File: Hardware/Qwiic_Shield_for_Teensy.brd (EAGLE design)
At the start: 17.8 x 61 mm, 42 parts, among them J1 QWIIC_RA, J2 QWIIC_RA, J3 QWIIC_Vertical, J4 QWIIC_Vertical, J5 ALT PWR

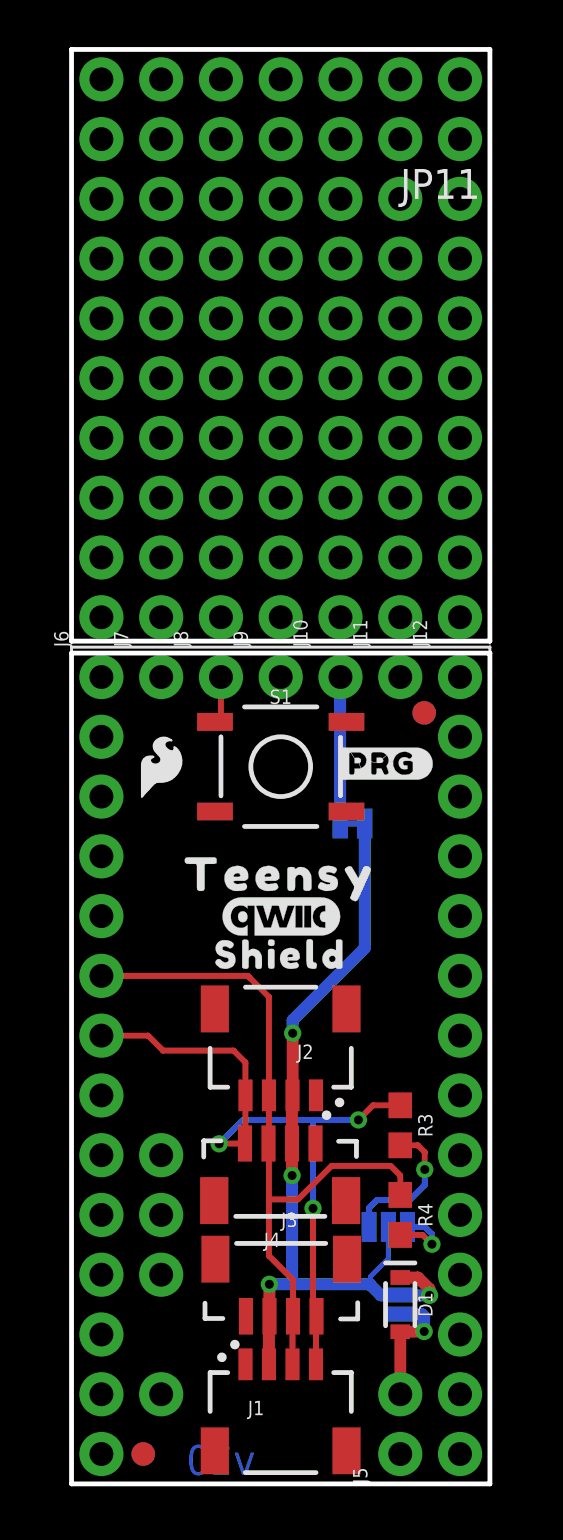
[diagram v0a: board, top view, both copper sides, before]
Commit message: Post group review changes - short version
-"slave" terminology needs to be updated to "I2C peripheral"
-Moving to two separate products. One short and one long. Resolves the prog button access pin difference. no vscores.
-Switch up qwiic connector positions so that the north RA connector doesn't conflict with the prog button.
-3.3V power should come from the PTH header pin on the side (not the middle row).
-Added teensy qwiic shield product name to bottom silk
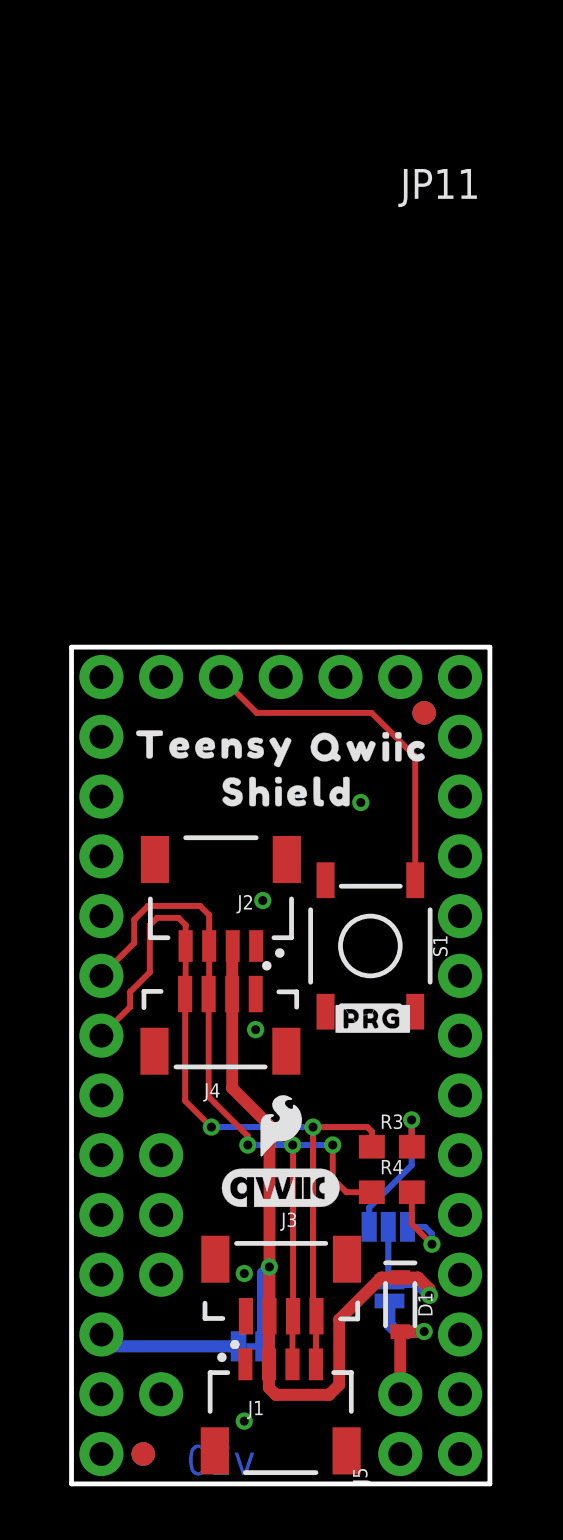
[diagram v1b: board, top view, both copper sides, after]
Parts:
- removed J10, J11, J12, J6, J7, J8, J9: (no value), SparkFun-Connectors:1X10_NO_SILK
- removed U$14: (no value), output:SHIELD0
- removed U$17: (no value), output:#GND#0
- added U$10: (no value), output:#ISO#0
- added U$11, U$9: (no value), output:QWIIC0
- added U$12, U$8: (no value), output:SHIELD0
- U$2: device output:#3V3_ISO#0 -> output:TEENSY0
- moved U$15 28.0 mm to (5.92, 6.38), turned to 0 degrees
- moved 3V3_ISO 22.6 mm to (7.62, 5.84)
- moved LOGO2 16.1 mm to (8.89, 15.2)
- moved LOGO4 11.5 mm to (8.86, 12.6)
- moved U$6 10.9 mm to (12.8, 19.8)
- moved LOGO1 9.26 mm to (8.94, 28.8), turned to 0 degrees
- moved S1 8.52 mm to (12.7, 22.9), turned to 270 degrees
- moved J4 6.84 mm to (6.35, 21.6)
- moved J2 6.84 mm to (6.35, 22.9)
- moved U$13 6.16 mm to (6.15, 31.4)
- moved LOGO3 5.11 mm to (8.89, 17.8), turned to 0 degrees
- moved U$2 1.52 mm to (11.7, 26.7)
- moved R4 1.03 mm to (13.6, 12.4), turned to 0 degrees
- moved R3 0.98 mm to (13.6, 14.3), turned to 0 degrees
- moved D1_BP 0.72 mm to (13.5, 8.18)
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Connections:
- removed net 3V: JP11.3V
- new net NC: JP11.3.3V
- net N$3: now also JP11.3V; no longer JP11.3.3V
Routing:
- net N$5: track 2.01 -> 14.9 mm
- net SCL: track 30.0 -> 34.1 mm, vias 3 -> 2
- net 3.3V: track 35.8 -> 38.4 mm, vias 4 -> 2
- net SDA: track 30.7 -> 33.3 mm, vias 0 -> 3
- net N$1: track 3.11 -> 4.16 mm
- net N$4: track 5.37 -> 6.28 mm
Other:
- board size 17.8 x 61 mm -> 17.8 x 35.6 mm

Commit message: Library updates, name prefix fix, measures update
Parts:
- removed JP11: TEENSY, SparkFun-Boards:TEENSY-3.1_NOSILK
- added J6: ALT PWR, SparkFun-Connectors:1X02_NO_SILK
- J1: value QWIIC_RA -> TEENSY; device SparkFun-Connectors:JST04_1MM_RA -> teensy_boards:TEENSY_NOSILK
- J3: value QWIIC_Vertical -> QWIIC_RA; device SparkFun-Connectors:JST04_1MM_VERT -> SparkFun-Connectors:JST04_1MM_RA
- J5: value ALT PWR -> QWIIC_Vertical; device SparkFun-Connectors:1X02_NO_SILK -> SparkFun-Connectors:JST04_1MM_VERT
- moved J5 21.7 mm to (6.35, 21.6), turned to 180 degrees
- moved J2 18.0 mm to (8.89, 5.08), turned to 0 degrees
- moved J3 16.7 mm to (6.35, 22.9), turned to 180 degrees
- moved J4 15.5 mm to (8.89, 6.35), turned to 0 degrees
- moved J1 12.7 mm to (8.89, 17.8)
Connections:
- net 3.3V: now also J5.2; no longer J1.2
- net GND: now also J1.AGND, J1.GND, J1.GND1, J6.1; no longer J1.1, JP11.AGND, JP11.GND, JP11.GND1
- net N$3: now also J1.3V; no longer JP11.3V
- net N$4: now also J6.2; no longer J5.2
- net N$5: now also J1.PROG; no longer JP11.PROG
- net NC: now also J1.3.3V; no longer JP11.3.3V
- net SCL: now also J1.19, J5.4; no longer J1.4, JP11.19
- net SDA: now also J1.18, J5.3; no longer J1.3, JP11.18
- net VBAT: now also J1.VBAT; no longer JP11.VBAT
- net VIN: now also J1.VIN; no longer JP11.VIN
- net VUSB: now also J1.VUSB; no longer JP11.VUSB
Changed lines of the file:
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@@
 <drawing>
 <settings>
-<setting alwaysvectorfont="yes"/>
+<setting alwaysvectorfont="no"/>
 <setting verticaltext="up"/>
 </settings>
@@
 <layer number="45" name="Holes" color="7" fill="1" visible="yes" active="yes"/>
 <layer number="46" name="Milling" color="3" fill="1" visible="no" active="yes"/>
-<layer number="47" name="Measures" color="7" fill="1" visible="no" active="yes"/>
+<layer number="47" name="Measures" color="7" fill="1" visible="yes" active="yes"/>
 <layer number="48" name="Document" color="7" fill="1" visible="no" active="yes"/>
 <layer number="49" name="Reference" color="7" fill="1" visible="yes" active="yes"/>
@@
 <wire x1="0" y1="35.56" x2="0" y2="0" width="0.2032" layer="20"/>
 <wire x1="0" y1="35.56" x2="17.78" y2="35.56" width="0.2032" layer="20"/>
-<dimension x1="0" y1="0" x2="0" y2="60.96" x3="-22.86" y3="30.48" textsize="1.778" layer="47" unit="inch" visible="yes"/>
-<dimension x1="0" y1="0" x2="0" y2="35.56" x3="-17.78" y3="17.78" textsize="1.778" layer="47" unit="inch" visible="yes"/>
-<dimension x1="0" y1="60.96" x2="17.78" y2="60.96" x3="8.89" y3="68.58" textsize="1.778" layer="47" unit="inch" visible="yes"/>
-<dimension x1="8.89" y1="30.48" x2="8.89" y2="0" x3="-12.7" y3="15.24" textsize="1.778" layer="47" unit="inch" visible="yes"/>
+<dimension x1="0" y1="0" x2="0" y2="35.56" x3="-22.86" y3="17.78" textsize="1.778" layer="47" unit="inch" visible="yes"/>
+<dimension x1="0" y1="35.56" x2="17.78" y2="35.56" x3="8.89" y3="49.53" textsize="1.778" layer="47" unit="inch" visible="yes"/>
 <dimension x1="9.271" y1="8.9408" x2="9.271" y2="0" x3="-2.54" y3="4.4704" textsize="1.27" layer="47" unit="inch" visible="yes"/>
-<dimension x1="9.271" y1="13.1064" x2="9.271" y2="0" x3="-7.747" y3="6.5532" textsize="1.27" layer="47" unit="inch" visible="yes"/>
 <rectangle x1="13.208" y1="0.5842" x2="15.9512" y2="1.9558" layer="22"/>
+<dimension x1="12.7" y1="22.86" x2="17.78" y2="0" x3="39.37" y3="11.43" textsize="1.778" layer="47" dtype="vertical" unit="inch" visible="yes"/>
+<dimension x1="12.7" y1="22.86" x2="0" y2="38.1" x3="6.35" y3="45.72" textsize="1.778" layer="47" dtype="horizontal" unit="inch" visible="yes"/>
+<dimension x1="6.35" y1="22.86" x2="0" y2="41.91" x3="3.175" y3="38.1" textsize="1.778" layer="47" dtype="horizontal" unit="inch" visible="yes"/>
+<dimension x1="6.5278" y1="25.3746" x2="-12.7" y2="0" x3="-11.43" y3="12.6873" textsize="1.778" layer="47" dtype="vertical" unit="inch" visible="yes"/>
+<dimension x1="6.3754" y1="19.0246" x2="-6.35" y2="0" x3="-16.51" y3="9.5123" textsize="1.778" layer="47" dtype="vertical" unit="inch" visible="yes"/>
 </plain>
 <attributes>
@@
 <attribute name="REV" value="" x="-12.7" y="-12.7" size="1.778" layer="27" display="off"/>
 </element>
-<element name="J1" library="SparkFun-Connectors" package="JST04_1MM_RA" value="QWIIC_RA" x="8.89" y="5.08" smashed="yes">
+<element name="J2" library="SparkFun-Connectors" package="JST04_1MM_RA" value="QWIIC_RA" x="8.89" y="5.08" smashed="yes">
 <attribute name="NAME" x="7.493" y="2.921" size="0.6096" layer="25" font="vector" ratio="20"/>
 <attribute name="PROD_ID" value="CONN-13694" x="8.89" y="5.08" size="1.778" layer="27" display="off"/>
 <attribute name="VALUE" x="7.239" y="1.778" size="0.6096" layer="27" font="vector" ratio="20"/>
 </element>
-<element name="J2" library="SparkFun-Connectors" package="JST04_1MM_RA" value="QWIIC_RA" x="6.35" y="22.86" smashed="yes" rot="R180">
+<element name="J3" library="SparkFun-Connectors" package="JST04_1MM_RA" value="QWIIC_RA" x="6.35" y="22.86" smashed="yes" rot="R180">
 <attribute name="NAME" x="7.747" y="25.019" size="0.6096" layer="25" font="vector" ratio="20" rot="R180"/>
 <attribute name="PROD_ID" value="CONN-13694" x="6.35" y="22.86" size="1.778" layer="27" rot="R180" display="off"/>
 <attribute name="VALUE" x="8.001" y="26.162" size="0.6096" layer="27" font="vector" ratio="20" rot="R180"/>
 </element>
-<element name="J4" library="SparkFun-Connectors" package="JST04_1MM_VERT" value="QWIIC_Vertical" x="6.35" y="21.59" smashed="yes" rot="R180">
+<element name="J5" library="SparkFun-Connectors" package="JST04_1MM_VERT" value="QWIIC_Vertical" x="6.35" y="21.59" smashed="yes" rot="R180">
 <attribute name="NAME" x="6.334" y="17.02366875" size="0.6096" layer="25" rot="R180"/>
 <attribute name="PROD_ID" value="CONN-14483" x="6.35" y="21.59" size="1.778" layer="27" rot="R180" display="off"/>
@@
 <element name="FD4" library="SparkFun-Aesthetics" package="FIDUCIAL-1X2" value="FIDUCIAL1X2" x="14.986" y="32.766" smashed="yes" rot="MR0"/>
 <element name="U$3" library="buzzard_labels (24)" package="3V36" value="" x="0" y="0" smashed="yes"/>
-<element name="JP11" library="SparkFun-Boards" package="TEENSY-3.1_NOSILK" value="TEENSY" x="8.89" y="17.78" smashed="yes">
+<element name="J1" library="teensy_boards" package="TEENSY_NOSILK" value="TEENSY" x="8.89" y="17.78" smashed="yes">
 <attribute name="NAME" x="13.97" y="54.61" size="1.27" layer="25"/>
 <attribute name="SF_ID" value="DEV-12646" x="8.89" y="17.78" size="1.778" layer="27" display="off"/>
@@
 <element name="LOGO4" library="SparkFun-Aesthetics" package="QWIIC_5MM" value="QWIIC_LOGO_5MM" x="8.8646" y="12.5984" smashed="yes"/>
 <element name="LOGO2" library="SparkFun-Aesthetics" package="SFE_LOGO_FLAME_.1" value="SFE_LOGO_FLAME.1_INCH" x="8.89" y="15.24" smashed="yes"/>
-<element name="J3" library="SparkFun-Connectors" package="JST04_1MM_VERT" value="QWIIC_Vertical" x="8.89" y="6.35" smashed="yes">
+<element name="J4" library="SparkFun-Connectors" package="JST04_1MM_VERT" value="QWIIC_Vertical" x="8.89" y="6.35" smashed="yes">
 <attribute name="NAME" x="8.906" y="10.91633125" size="0.6096" layer="25"/>
 <attribute name="PROD_ID" value="CONN-14483" x="0" y="15.24" size="1.778" layer="27" font="vector" ratio="15" display="off"/>
@@
 <element name="U$18" library="output" package="#SDA#0" value="" x="1.778" y="21.59" smashed="yes" rot="MR0"/>
 <element name="U$19" library="output" package="#SCL#0" value="" x="1.7526" y="19.0754" smashed="yes" rot="MR0"/>
-<element name="J5" library="SparkFun-Connectors" package="1X02_NO_SILK" value="ALT PWR" x="13.97" y="1.27" smashed="yes" rot="R90">
+<element name="J6" library="SparkFun-Connectors" package="1X02_NO_SILK" value="ALT PWR" x="13.97" y="1.27" smashed="yes" rot="R90">
 <attribute name="NAME" x="12.573" y="0" size="0.6096" layer="25" font="vector" ratio="20" rot="R90"/>
 <attribute name="VALUE" x="16.002" y="0" size="0.6096" layer="27" font="vector" ratio="20" rot="R90"/>
@@
 <signals>
 <signal name="GND">
-<contactref element="J4" pad="1"/>
+<contactref element="J5" pad="1"/>
+<contactref element="J3" pad="1"/>
 <contactref element="J2" pad="1"/>
-<contactref element="J1" pad="1"/>
 <polygon width="0.2032" layer="1" isolate="0.2032">
 <vertex x="0" y="0"/>
@@
 <vertex x="17.78" y="35.56"/>
 </polygon>
-<contactref element="JP11" pad="GND"/>
-<contactref element="JP11" pad="GND1"/>
-<contactref element="JP11" pad="AGND"/>
-<contactref element="J3" pad="1"/>
-<contactref element="J5" pad="1"/>
+<contactref element="J1" pad="GND"/>
+<contactref element="J1" pad="GND1"/>
+<contactref element="J1" pad="AGND"/>
+<contactref element="J4" pad="1"/>
+<contactref element="J6" pad="1"/>
 <contactref element="S1" pad="3"/>
 <via x="12.2936" y="28.956" extent="1-16" drill="0.381"/>
@@
 </signal>
 <signal name="3.3V">
-<contactref element="J1" pad="2"/>
 <contactref element="J2" pad="2"/>
+<contactref element="J3" pad="2"/>
+<contactref element="J5" pad="2"/>
+<contactref element="I2C" pad="2"/>
 <contactref element="J4" pad="2"/>
-<contactref element="I2C" pad="2"/>
-<contactref element="J3" pad="2"/>
 <contactref element="3V3_ISO" pad="1"/>
 <contactref element="D1_BP" pad="2"/>
@@
 </signal>
 <signal name="SDA">
-<contactref element="J1" pad="3"/>
 <contactref element="J2" pad="3"/>
+<contactref element="J3" pad="3"/>
+<contactref element="J5" pad="3"/>
+<contactref element="R4" pad="1"/>
+<contactref element="J1" pad="18"/>
 <contactref element="J4" pad="3"/>
-<contactref element="R4" pad="1"/>
-<contactref element="JP11" pad="18"/>
-<contactref element="J3" pad="3"/>
 <wire x1="9.39" y1="5.08" x2="9.39" y2="7.103" width="0.254" layer="1"/>
 <wire x1="9.39" y1="7.103" x2="9.412" y2="7.125" width="0.254" layer="1"/>
@@
 </signal>
 <signal name="SCL">
-<contactref element="J1" pad="4"/>
 <contactref element="J2" pad="4"/>
+<contactref element="J3" pad="4"/>
+<contactref element="J5" pad="4"/>
+<contactref element="R3" pad="1"/>
+<contactref element="J1" pad="19"/>
 <contactref element="J4" pad="4"/>
-<contactref element="R3" pad="1"/>
-<contactref element="JP11" pad="19"/>
-<contactref element="J3" pad="4"/>
 <wire x1="10.39" y1="5.08" x2="10.39" y2="7.103" width="0.254" layer="1"/>
 <wire x1="10.39" y1="7.103" x2="10.412" y2="7.125" width="0.254" layer="1"/>
@@
 </signal>
 <signal name="N$4">
-<contactref element="J5" pad="2"/>
+<contactref element="J6" pad="2"/>
 <contactref element="D1_BP" pad="1"/>
 <contactref element="D1" pad="A"/>
@@
 </signal>
 <signal name="N$5">
-<contactref element="JP11" pad="PROG"/>
+<contactref element="J1" pad="PROG"/>
 <contactref element="S1" pad="1"/>
 <wire x1="14.605" y1="25.654" x2="14.605" y2="30.9118" width="0.254" layer="1"/>
@@
 </signal>
 <signal name="VBAT">
-<contactref element="JP11" pad="VBAT"/>
+<contactref element="J1" pad="VBAT"/>
 </signal>
 <signal name="VIN">
-<contactref element="JP11" pad="VIN"/>
+<contactref element="J1" pad="VIN"/>
 </signal>
 <signal name="VUSB">
-<contactref element="JP11" pad="VUSB"/>
+<contactref element="J1" pad="VUSB"/>
 </signal>
 <signal name="N$3">
-<contactref element="JP11" pad="3V"/>
+<contactref element="J1" pad="3V"/>
 <contactref element="3V3_ISO" pad="2"/>
 <wire x1="7.0993" y1="5.842" x2="1.778" y2="5.842" width="0.508" layer="16"/>
@@
 </signal>
 <signal name="NC">
-<contactref element="JP11" pad="3.3V"/>
+<contactref element="J1" pad="3.3V"/>
 </signal>
 </signals>
